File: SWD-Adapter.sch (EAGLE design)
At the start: 5 parts

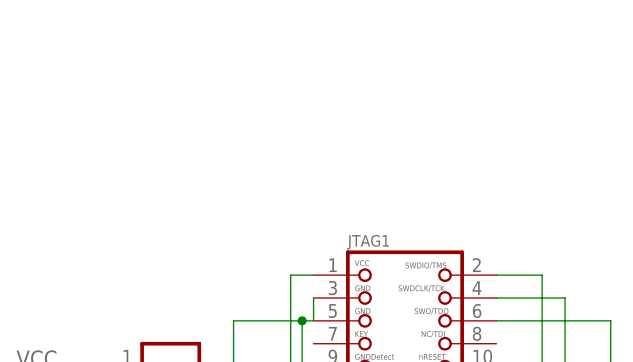
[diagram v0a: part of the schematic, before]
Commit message: add 6pin TC2030 pinout to SWD-Adapter variant
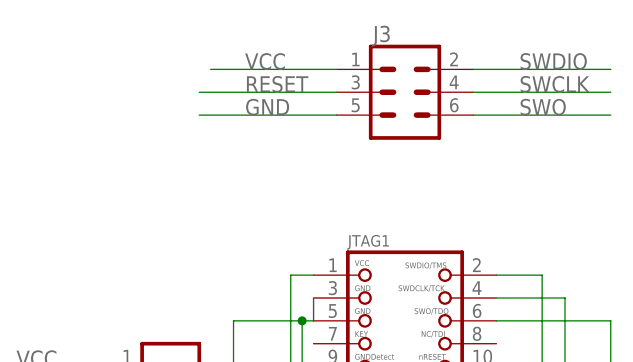
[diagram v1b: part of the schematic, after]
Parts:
- added J3: (no value), SparkFun-Connectors:CONN_03X2NO_SILK
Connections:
- net GND: now also J3.5
- net RESET: now also J3.3
- net SWCLK: now also J3.4
- net SWDIO: now also J3.2
- net SWO: now also J3.6
- net VCC: now also J3.1
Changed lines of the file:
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@@
 <setting verticaltext="up"/>
 </settings>
-<grid distance="0.05" unitdist="inch" unit="inch" style="lines" multiple="1" display="no" altdistance="0.01" altunitdist="inch" altunit="inch"/>
+<grid distance="0.1" unitdist="inch" unit="inch" style="lines" multiple="1" display="no" altdistance="0.01" altunitdist="inch" altunit="inch"/>
 <layers>
 <layer number="1" name="Top" color="4" fill="1" visible="no" active="no"/>
@@
 <part name="JTAG3" library="microbuilder" library_urn="urn:adsk.eagle:library:25095254" deviceset="JTAG-CORTEXM3" device="MOLEX20" package3d_urn="urn:adsk.eagle:package:25096088/1"/>
 <part name="J1" library="SparkFun-Connectors" deviceset="CONN_06" device="SILK_FEMALE_PTH"/>
+<part name="J3" library="SparkFun-Connectors" deviceset="CONN_03X2" device="NO_SILK"/>
 </parts>
 <sheets>
@@
 <attribute name="VALUE" x="13.97" y="25.146" size="1.778" layer="96" font="vector" rot="R180"/>
 <attribute name="NAME" x="13.97" y="4.572" size="1.778" layer="95" font="vector" rot="R180"/>
+</instance>
+<instance part="J3" gate="G$1" x="60.96" y="50.8" smashed="yes">
+<attribute name="NAME" x="57.404" y="56.388" size="1.778" layer="95" font="vector"/>
+<attribute name="VALUE" x="57.658" y="44.958" size="1.778" layer="96" font="vector" align="top-left"/>
 </instance>
 </instances>
@@
 <junction x="83.82" y="-12.7"/>
 <pinref part="J1" gate="G$1" pin="6"/>
+</segment>
+<segment>
+<wire x1="68.58" y1="48.26" x2="83.82" y2="48.26" width="0.1524" layer="91"/>
+<label x="73.66" y="48.26" size="1.778" layer="95"/>
+<pinref part="J3" gate="G$1" pin="6"/>
 </segment>
 </net>
@@
 <pinref part="J1" gate="G$1" pin="5"/>
 </segment>
+<segment>
+<wire x1="38.1" y1="48.26" x2="53.34" y2="48.26" width="0.1524" layer="91"/>
+<label x="43.18" y="48.26" size="1.778" layer="95"/>
+<pinref part="J3" gate="G$1" pin="5"/>
+</segment>
 </net>
 <net name="SWCLK" class="0">
@@
 <pinref part="J1" gate="G$1" pin="4"/>
 </segment>
+<segment>
+<wire x1="68.58" y1="50.8" x2="83.82" y2="50.8" width="0.1524" layer="91"/>
+<label x="73.66" y="50.8" size="1.778" layer="95"/>
+<pinref part="J3" gate="G$1" pin="4"/>
+</segment>
 </net>
 <net name="RESET" class="0">
@@
 <pinref part="J1" gate="G$1" pin="3"/>
 </segment>
+<segment>
+<wire x1="38.1" y1="50.8" x2="53.34" y2="50.8" width="0.1524" layer="91"/>
+<label x="43.18" y="50.8" size="1.778" layer="95"/>
+<pinref part="J3" gate="G$1" pin="3"/>
+</segment>
 </net>
 <net name="SWDIO" class="0">
@@
 <pinref part="J1" gate="G$1" pin="2"/>
 </segment>
+<segment>
+<wire x1="68.58" y1="53.34" x2="83.82" y2="53.34" width="0.1524" layer="91"/>
+<label x="73.66" y="53.34" size="1.778" layer="95"/>
+<pinref part="J3" gate="G$1" pin="2"/>
+</segment>
 </net>
 <net name="VCC" class="0">
@@
 <pinref part="J1" gate="G$1" pin="1"/>
 </segment>
-</net>
+<segment>
+<wire x1="39.37" y1="53.34" x2="53.34" y2="53.34" width="0.1524" layer="91"/>
+<label x="43.18" y="53.34" size="1.778" layer="95"/>
+<pinref part="J3" gate="G$1" pin="1"/>
+</segment>
+</net>
